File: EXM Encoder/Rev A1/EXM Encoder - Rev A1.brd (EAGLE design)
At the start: 30 x 35 mm, 8 parts, among them J2 22-05-7058-05, T1 EXMACHINA-LOGO-NAME

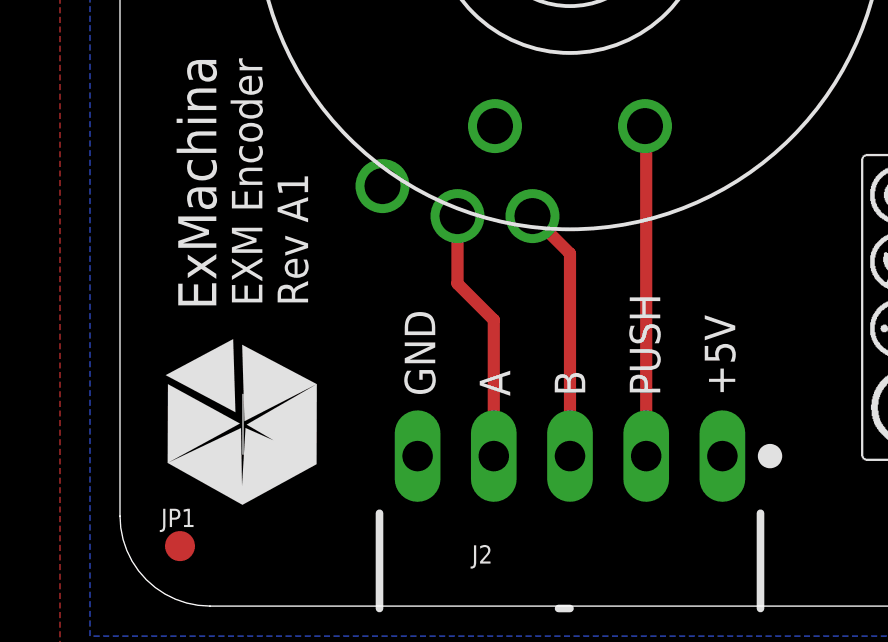
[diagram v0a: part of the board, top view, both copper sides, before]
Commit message: Update schematic and board due to the update of encoder symbol
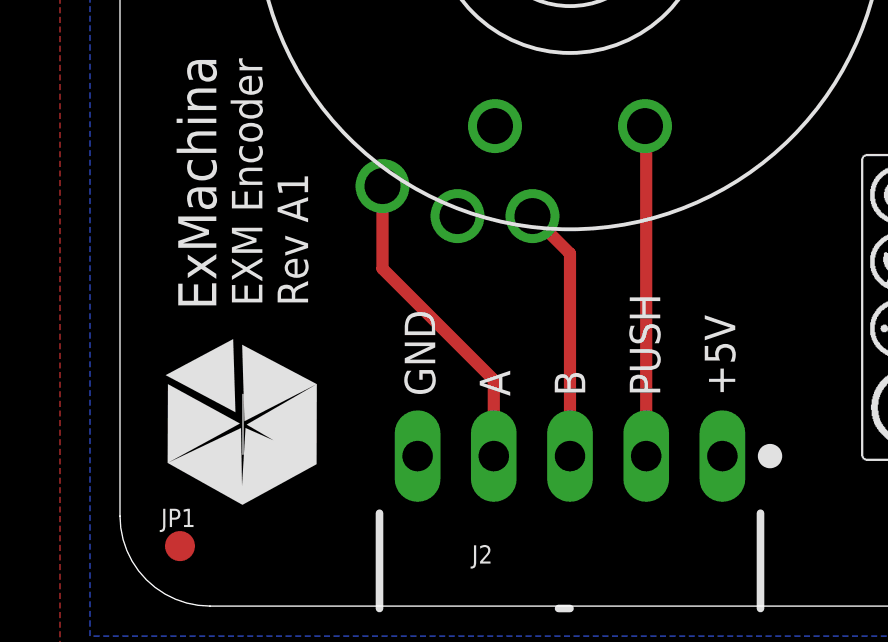
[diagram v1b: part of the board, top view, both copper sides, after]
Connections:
- net ENCODER_A: now also E1.A; no longer E1.C
- net GND: now also E1.C; no longer E1.A
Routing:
- net ENCODER_A: track 8.50 -> 10.5 mm
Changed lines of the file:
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@@
 <signal name="GND">
 <contactref element="E1" pad="D"/>
-<contactref element="E1" pad="A"/>
+<contactref element="E1" pad="C"/>
 <contactref element="J2" pad="5"/>
 <polygon width="0.4064" layer="1">
@@
 </signal>
 <signal name="ENCODER_A">
-<contactref element="E1" pad="C"/>
+<contactref element="E1" pad="A"/>
 <contactref element="J2" pad="4"/>
-<wire x1="12.46" y1="5" x2="12.46" y2="9.54" width="0.4064" layer="1"/>
-<wire x1="12.46" y1="9.54" x2="11.25" y2="10.75" width="0.4064" layer="1"/>
-<wire x1="11.25" y1="10.75" x2="11.25" y2="13" width="0.4064" layer="1"/>
+<wire x1="12.46" y1="5" x2="12.46" y2="7.54" width="0.4064" layer="1"/>
+<wire x1="12.46" y1="7.54" x2="8.75" y2="11.25" width="0.4064" layer="1"/>
+<wire x1="8.75" y1="11.25" x2="8.75" y2="14" width="0.4064" layer="1"/>
 </signal>
 <signal name="ENCODER_B">
